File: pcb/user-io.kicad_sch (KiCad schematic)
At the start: 17 parts, among them J4 FH26-15S-0.3SHW(05), SW2 PEC12R-4222F-S0024, U150 SN74LVC1G14DBVR

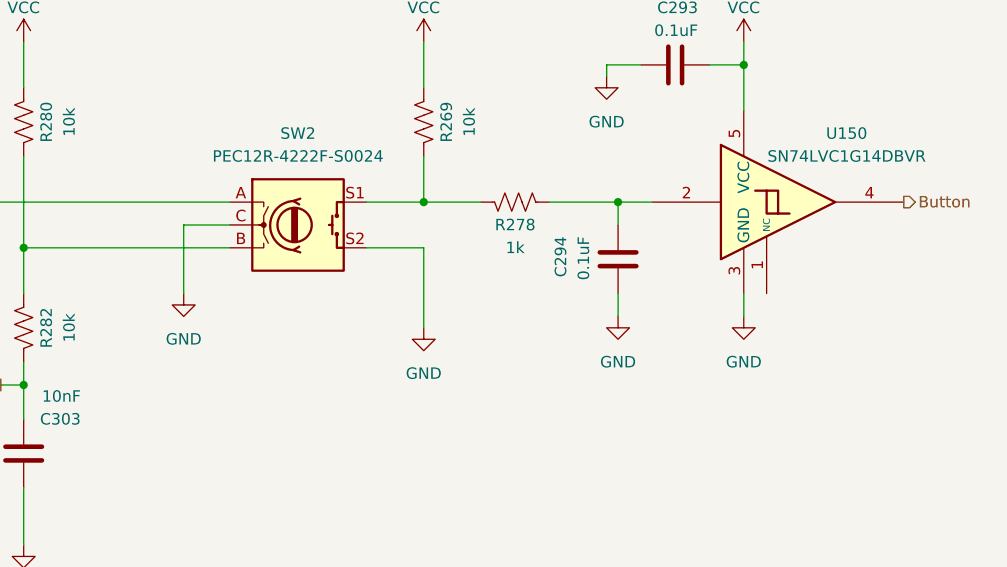
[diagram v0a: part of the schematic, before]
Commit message: Initial Rev. A schematic
- I think this has everything we need for revision A
- Battery charge indication via the OLED display
- User interface via rotary encoder/select switch
- Cycle through affected individual channels, none, or all
- Cycle through amplitudes
- Cycle through frequencies
- Select signal source
- Cycle through pre-loaded channel maps?
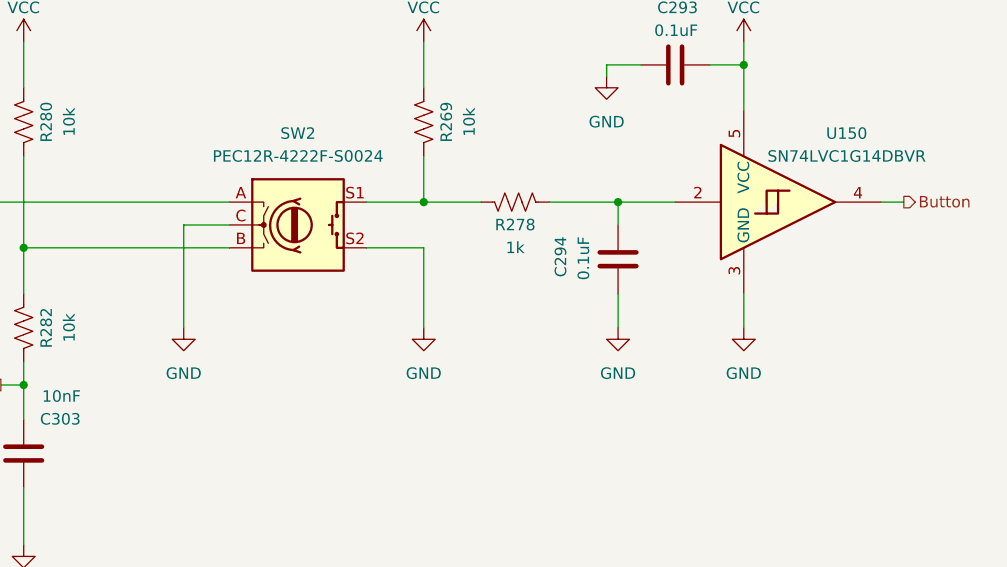
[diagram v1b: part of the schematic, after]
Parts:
- J4: Datasheet1 (none) -> https://mm.digikey.com/Volume0/opasdata/d220001/medias/docu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
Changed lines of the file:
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@@
 	(wire
 		(pts
+			(xy 204.47 130.81) (xy 207.01 130.81)
+		)
+		(stroke
+			(width 0)
+			(type default)
+		)
+	)
+	(wire
+		(pts
 			(xy 173.99 116.84) (xy 173.99 115.57)
 		)
@@
 	(wire
 		(pts
-			(xy 175.26 140.97) (xy 175.26 143.51)
+			(xy 175.26 140.97) (xy 175.26 144.78)
 		)
 		(stroke
@@
 	(wire
 		(pts
-			(xy 175.26 130.81) (xy 179.07 130.81)
+			(xy 175.26 130.81) (xy 181.61 130.81)
 		)
 		(stroke
@@
 	(wire
 		(pts
-			(xy 127 133.35) (xy 127 140.97)
+			(xy 127 133.35) (xy 127 144.78)
 		)
 		(stroke
@@
 	(wire
 		(pts
-			(xy 189.23 140.97) (xy 189.23 143.51)
+			(xy 189.23 140.97) (xy 189.23 144.78)
 		)
 		(stroke
@@
 	(label "~{D{slash}C}"
 		(at 149.86 48.26 0)
+		(fields_autoplaced yes)
 		(effects
 			(font
@@
 	(label "~{CS}"
 		(at 149.86 45.72 0)
+		(fields_autoplaced yes)
 		(effects
 			(font
@@
 	(label "MOSI"
 		(at 149.86 50.8 0)
+		(fields_autoplaced yes)
 		(effects
 			(font
@@
 			)
 		)
-		(property "Description" ""
+		(property "Description" "Power symbol creates a global label with name \"GND\" , ground"
 			(at 173.99 116.84 0)
 			(effects
@@
 			)
 		)
-		(property "Description" ""
+		(property "Description" "Unpolarized capacitor"
 			(at 109.22 158.75 0)
 			(effects
@@
 			)
 		)
-		(property "Datasheet" "https://mm.digikey.com/Volume0/opasdata/d220001/medias/docus/790/FH26-xxS-0.3SHW%2805%29_Dwg.pdf"
+		(property "Datasheet" "~"
 			(at 142.24 45.72 0)
 			(effects
@@
 			)
 		)
+		(property "Datasheet1" "https://mm.digikey.com/Volume0/opasdata/d220001/medias/docus/4998/MCOT128032CY-WS.pdf"
+			(at 142.24 45.72 0)
+			(effects
+				(font
+					(size 1.27 1.27)
+				)
+				(hide yes)
+			)
+		)
 		(pin "5"
 		)
@@
 			)
 		)
-		(property "Description" ""
+		(property "Description" "Power symbol creates a global label with name \"GND\" , ground"
 			(at 87.63 168.91 0)
 			(effects
@@
 	(symbol
 		(lib_id "power:GND")
-		(at 189.23 143.51 0)
+		(at 189.23 144.78 0)
 		(mirror y)
 		(unit 1)
@@
 		(fields_autoplaced yes)
 		(property "Reference" "#PWR0745"
-			(at 189.23 149.86 0)
+			(at 189.23 151.13 0)
 			(effects
 				(font
@@
 		)
 		(property "Value" "GND"
-			(at 189.23 148.59 0)
+			(at 189.23 149.86 0)
 			(effects
 				(font
@@
 		)
 		(property "Footprint" ""
-			(at 189.23 143.51 0)
+			(at 189.23 144.78 0)
 			(effects
 				(font
@@
 		)
 		(property "Datasheet" ""
-			(at 189.23 143.51 0)
+			(at 189.23 144.78 0)
 			(effects
 				(font
@@
 			)
 		)
-		(property "Description" ""
-			(at 189.23 143.51 0)
+		(property "Description" "Power symbol creates a global label with name \"GND\" , ground"
+			(at 189.23 144.78 0)
 			(effects
 				(font
@@
 			)
 		)
-		(property "Description" ""
+		(property "Description" "Power symbol creates a global label with name \"VPP\""
 			(at 113.03 35.56 0)
 			(effects
@@
 	(symbol
 		(lib_id "power:GND")
-		(at 175.26 143.51 0)
+		(at 175.26 144.78 0)
 		(mirror y)
 		(unit 1)
@@
 		(fields_autoplaced yes)
 		(property "Reference" "#PWR0750"
-			(at 175.26 149.86 0)
+			(at 175.26 151.13 0)
 			(effects
 				(font
@@
 		)
 		(property "Value" "GND"
-			(at 175.26 148.59 0)
+			(at 175.26 149.86 0)
 			(effects
 				(font
@@
 		)
 		(property "Footprint" ""
-			(at 175.26 143.51 0)
+			(at 175.26 144.78 0)
 			(effects
 				(font
@@
 		)
 		(property "Datasheet" ""
-			(at 175.26 143.51 0)
+			(at 175.26 144.78 0)
 			(effects
 				(font
@@
 			)
 		)
-		(property "Description" ""
-			(at 175.26 143.51 0)
+		(property "Description" "Power symbol creates a global label with name \"GND\" , ground"
+			(at 175.26 144.78 0)
 			(effects
 				(font
@@
 			)
 		)
-		(property "Description" ""
+		(property "Description" "Power symbol creates a global label with name \"GND\" , ground"
 			(at 153.67 144.78 0)
 			(effects
@@
 			)
 		)
-		(property "Description" ""
+		(property "Description" "Unpolarized capacitor"
 			(at 175.26 58.42 0)
 			(effects
@@
 	(symbol
 		(lib_id "power:GND")
-		(at 127 140.97 0)
+		(at 127 144.78 0)
 		(mirror y)
 		(unit 1)
@@
 		(fields_autoplaced yes)
 		(property "Reference" "#PWR0769"
-			(at 127 147.32 0)
+			(at 127 151.13 0)
 			(effects
 				(font
@@
 		)
 		(property "Value" "GND"
-			(at 127 146.05 0)
+			(at 127 149.86 0)
 			(effects
 				(font
@@
 		)
 		(property "Footprint" ""
-			(at 127 140.97 0)
+			(at 127 144.78 0)
 			(effects
 				(font
@@
 		)
 		(property "Datasheet" ""
-			(at 127 140.97 0)
+			(at 127 144.78 0)
 			(effects
 				(font
@@
 			)
 		)
-		(property "Description" ""
-			(at 127 140.97 0)
+		(property "Description" "Power symbol creates a global label with name \"GND\" , ground"
+			(at 127 144.78 0)
 			(effects
 				(font
@@
 			)
 		)
-		(property "Description" ""
+		(property "Description" "Power symbol creates a global label with name \"GND\" , ground"
 			(at 109.22 168.91 0)
 			(effects
@@
 			)
 		)
-		(property "Description" ""
+		(property "Description" "Unpolarized capacitor"
 			(at 175.26 137.16 0)
 			(effects
@@
 			)
 		)
-		(property "Datasheet" "https://www.ti.com/lit/ds/symlink/sn74lvc1g14.pdf?HQS=dis-dk-null-digikeymode-dsf-pf-null-wwe&ts=1731095042391&ref_url=https%253A%252F%252Fwww.ti.com%252Fgeneral%252Fdocs%252Fsuppproductinfo.tsp%253FdistId%253D10%2526gotoUrl%253Dhttps%253A%252F%252Fwww.ti.com%252Flit%252Fgpn%252Fsn74lvc1g14"
+		(property "Datasheet" "https://www.ti.com/lit/ds/symlink/sn74lvc1g17.pdf"
 			(at 194.31 130.81 0)
 			(effects
@@
 			)
 		)
-		(property "Description" ""
+		(property "Description" "Single Schmitt Buffer Gate, Low-Voltage CMOS"
 			(at 194.31 130.81 0)
 			(effects
@@
 			)
 		)
-		(property "Description" ""
+		(property "Description" "Unpolarized capacitor"
 			(at 87.63 158.75 0)
 			(effects
@@
 			)
 		)
-		(property "Description" ""
+		(property "Description" "Unpolarized capacitor"
 			(at 113.03 63.5 0)
 			(effects
@@
 			)
 		)
-		(property "Description" ""
+		(property "Description" "Unpolarized capacitor"
 			(at 181.61 115.57 0)
 			(effects
@@
 			)
 		)
-		(property "Datasheet" "https://www.bourns.com/docs/Product-Datasheets/PEC12R.pdf"
+		(property "Datasheet" "~"
 			(at 139.7 126.746 0)
 			(effects

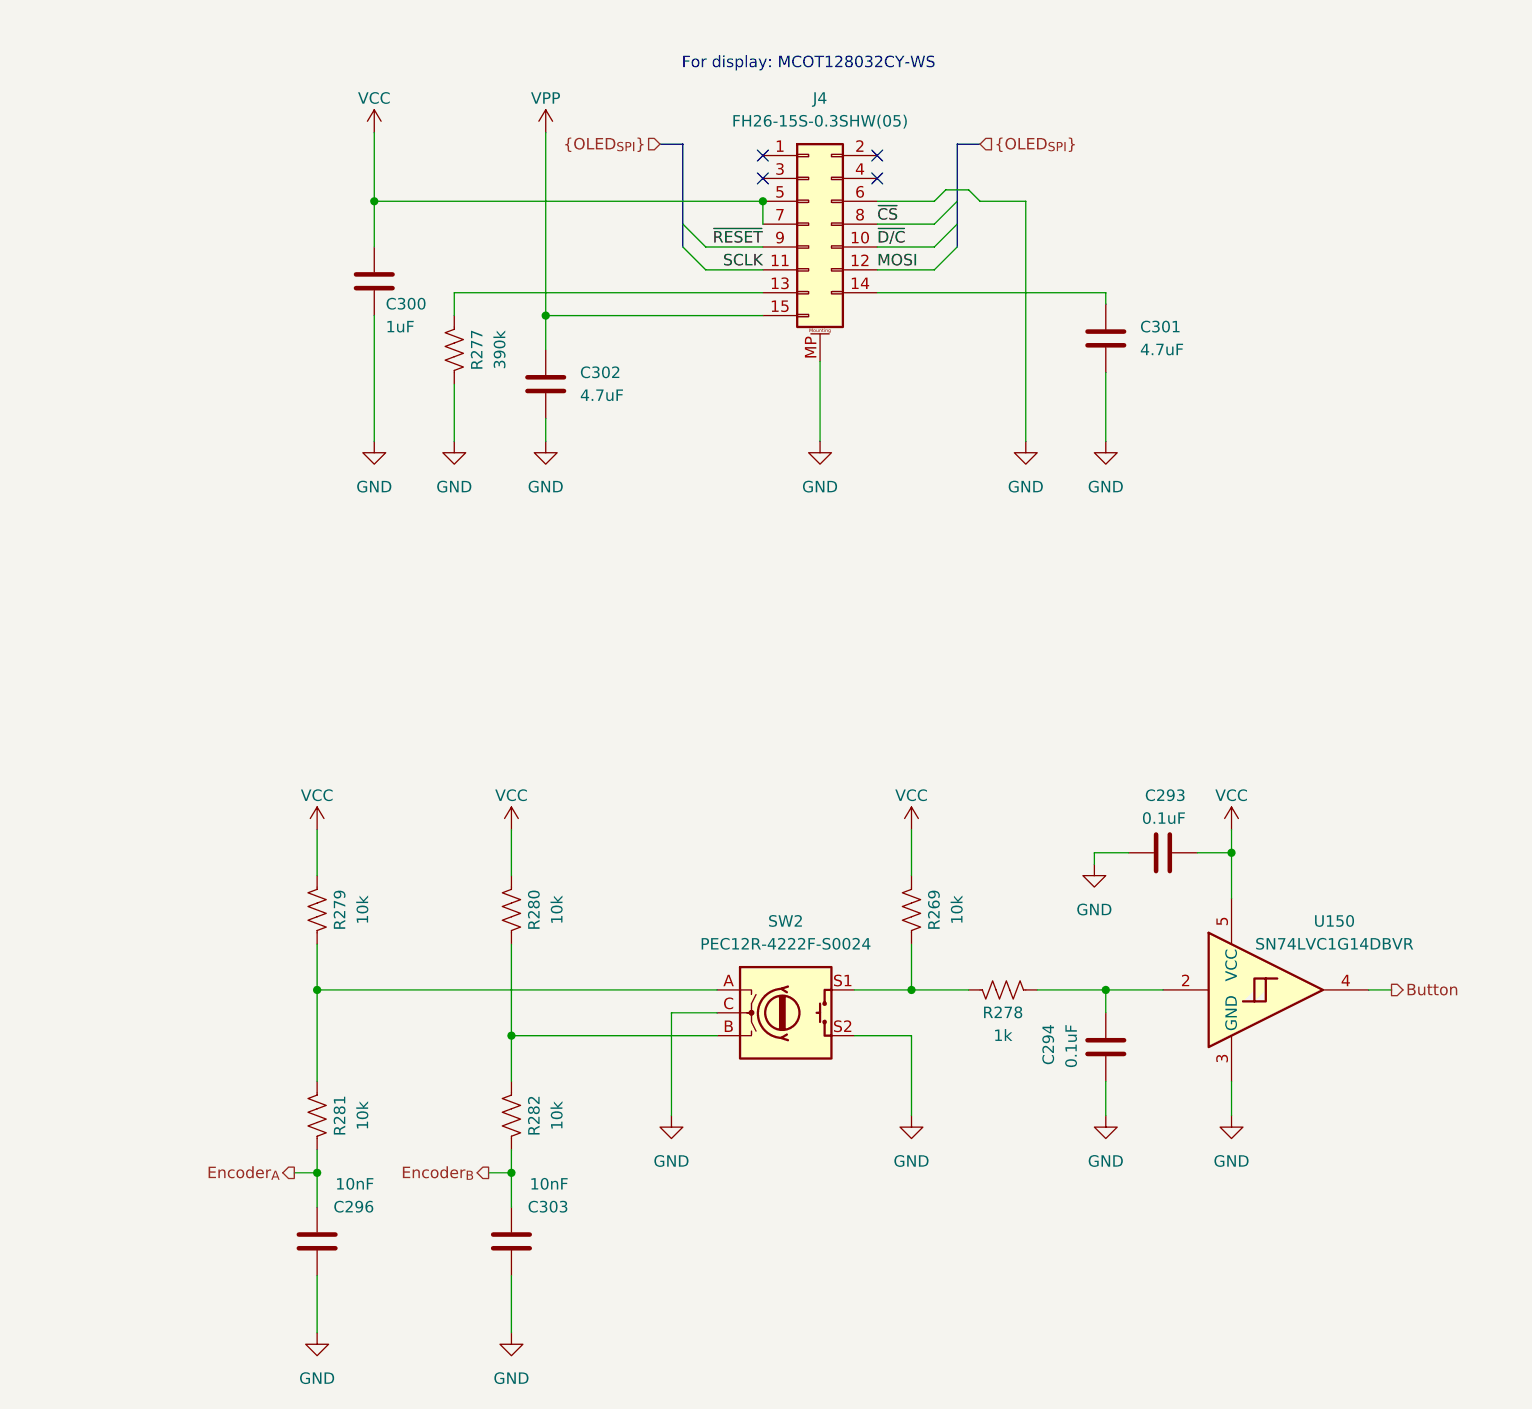
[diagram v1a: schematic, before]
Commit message: More schematic improvements
- Add pullups to i2c bus
- Add test points
- Ready for initial routing
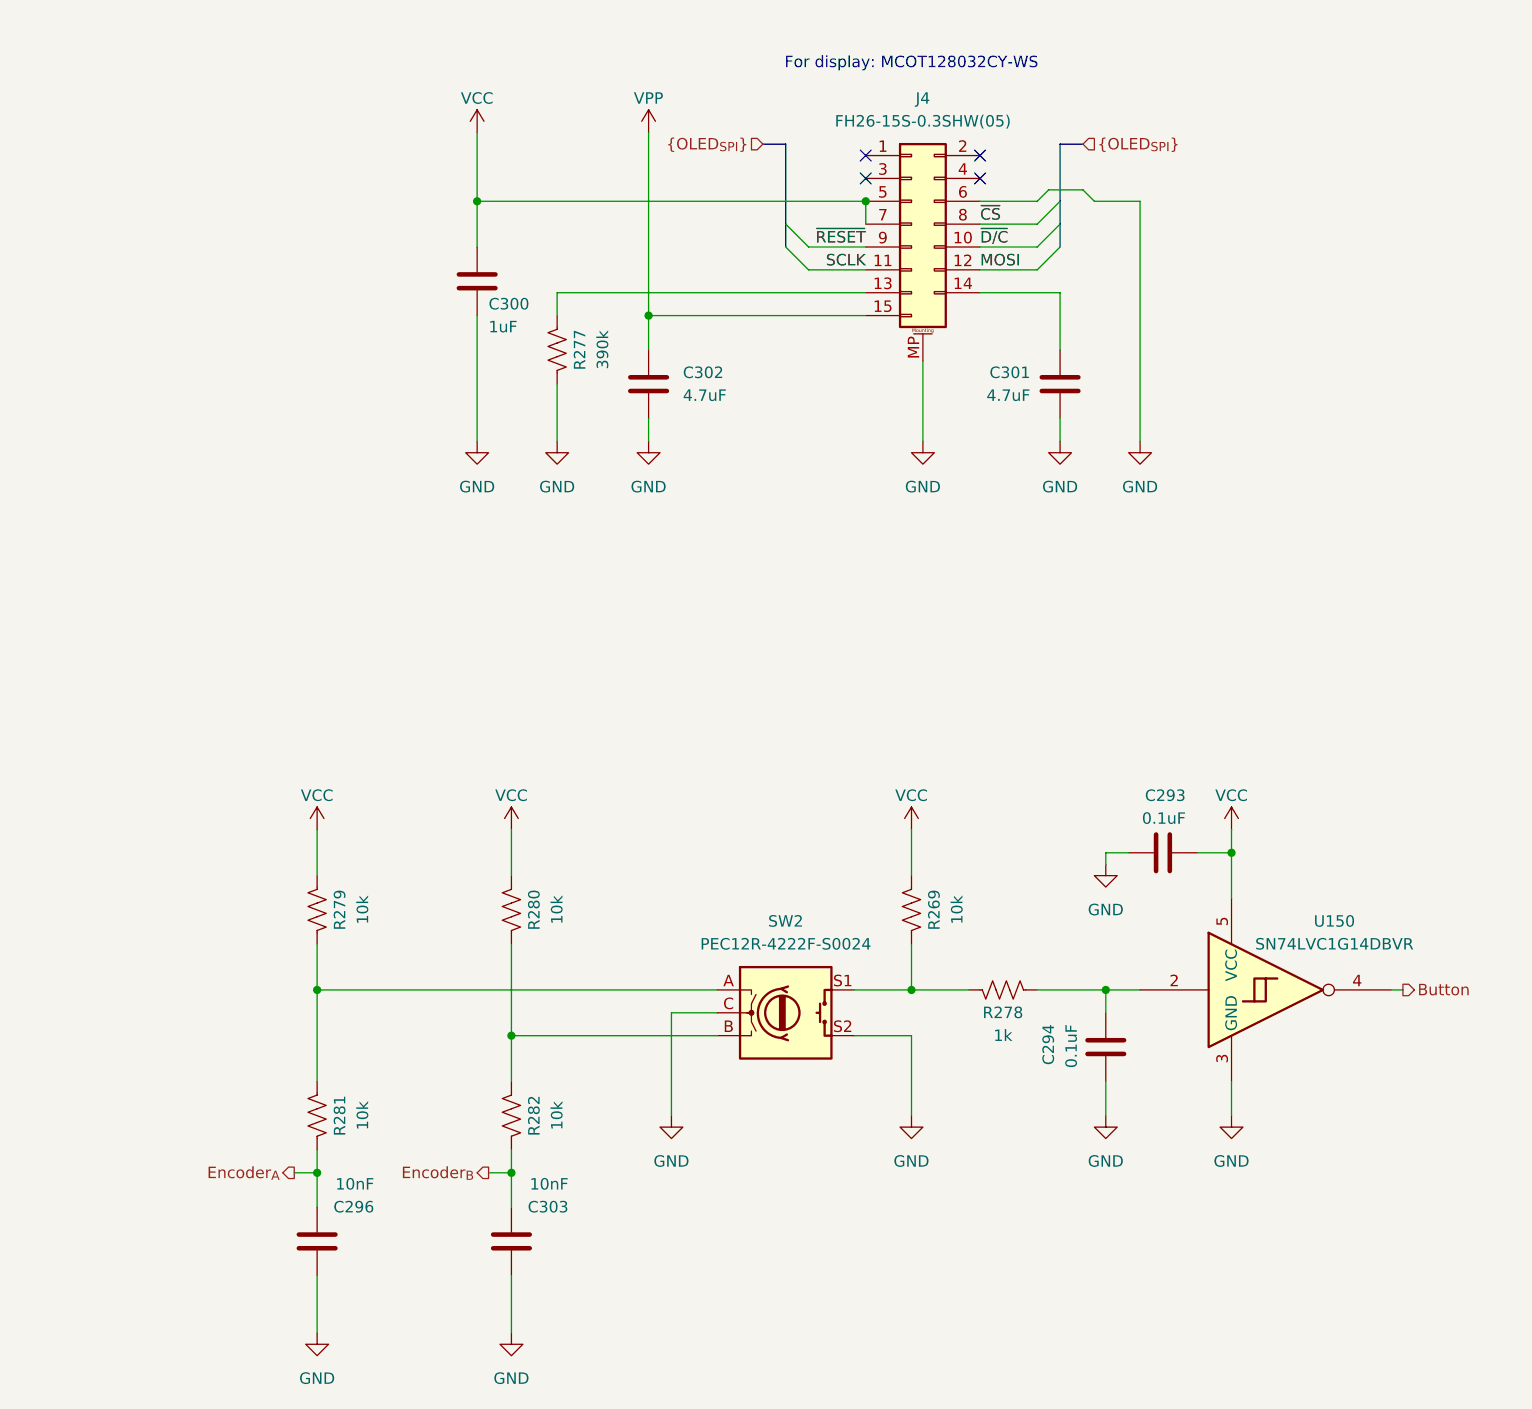
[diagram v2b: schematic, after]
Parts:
- U150: symbol 74xGxx:74LVC1G17 -> 74xGxx:74LVC1G14
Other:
- moved on the sheet: C300, C301, C302, J4, R277
